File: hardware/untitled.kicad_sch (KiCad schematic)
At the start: 7 parts, among them U2 H5TQ4G63EFR

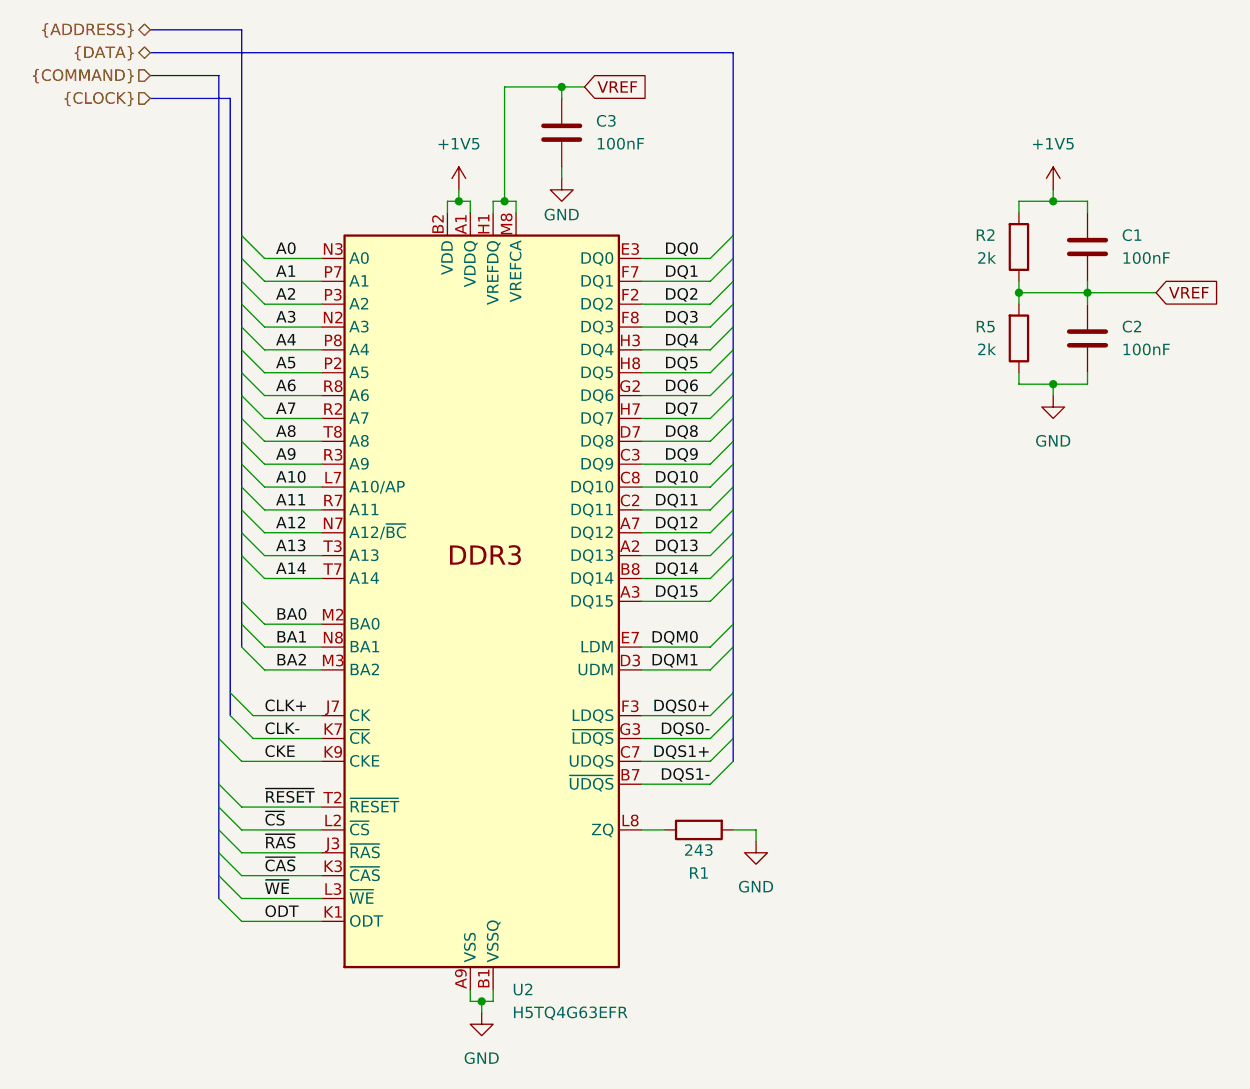
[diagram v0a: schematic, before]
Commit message: Added A13 line to DDR3
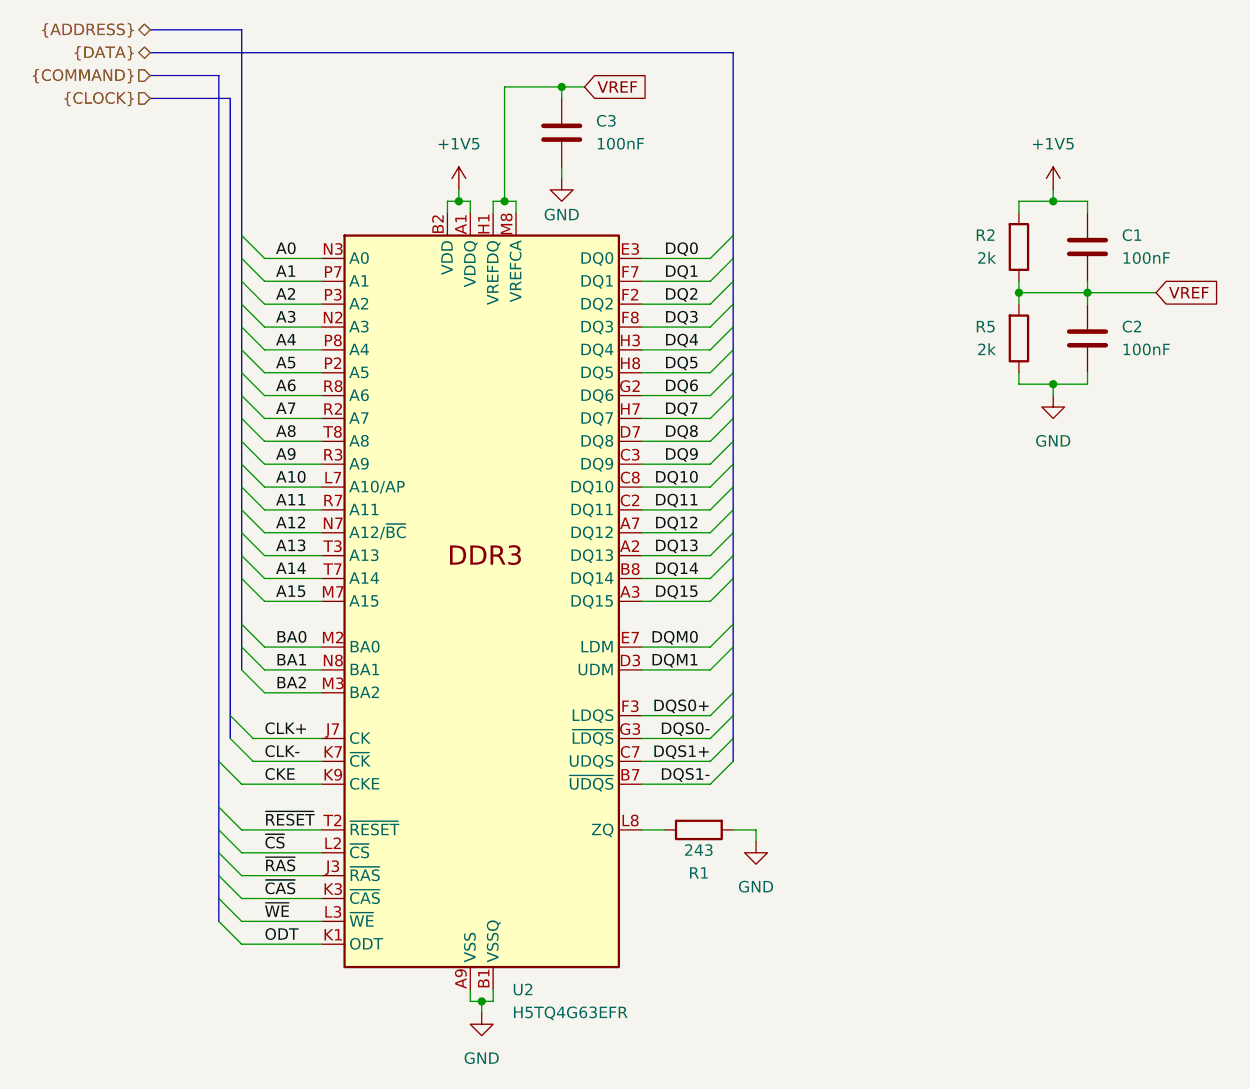
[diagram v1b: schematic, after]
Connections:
- net A15: now reaches U2.M7 (A15)
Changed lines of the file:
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@@
 	(paper "A4")
 	(bus_alias "ADDRESS"
-		(members "A[0..14]" "BA[0..2]")
+		(members "A[0..15]" "BA[0..2]")
 	)
 	(bus_alias "CLOCK"
@@
 	)
 	(bus_entry
-		(at 55.88 107.95)
+		(at 55.88 110.49)
 		(size -2.54 -2.54)
 		(stroke
@@
 	)
 	(bus_entry
-		(at 55.88 105.41)
+		(at 55.88 107.95)
 		(size -2.54 -2.54)
 		(stroke
@@
 	)
 	(bus_entry
-		(at 54.61 115.57)
+		(at 54.61 118.11)
 		(size -2.54 -2.54)
 		(stroke
@@
 	)
 	(bus_entry
-		(at 54.61 123.19)
+		(at 54.61 125.73)
 		(size -2.54 -2.54)
 		(stroke
@@
 	)
 	(bus_entry
-		(at 54.61 125.73)
+		(at 54.61 128.27)
 		(size -2.54 -2.54)
 		(stroke
@@
 	)
 	(bus_entry
-		(at 54.61 110.49)
+		(at 54.61 113.03)
 		(size -2.54 -2.54)
 		(stroke
@@
 	)
 	(bus_entry
-		(at 57.15 97.79)
+		(at 57.15 100.33)
 		(size -2.54 -2.54)
 		(stroke
@@
 	)
 	(bus_entry
-		(at 57.15 100.33)
+		(at 57.15 102.87)
 		(size -2.54 -2.54)
 		(stroke
@@
 	)
 	(bus_entry
-		(at 54.61 118.11)
+		(at 54.61 120.65)
 		(size -2.54 -2.54)
 		(stroke
@@
 	)
 	(bus_entry
-		(at 54.61 128.27)
+		(at 54.61 130.81)
+		(size -2.54 -2.54)
+		(stroke
+			(width 0)
+			(type default)
+		)
+	)
+	(bus_entry
+		(at 57.15 92.71)
 		(size -2.54 -2.54)
 		(stroke
@@
 	)
 	(bus_entry
-		(at 54.61 120.65)
+		(at 54.61 123.19)
 		(size -2.54 -2.54)
 		(stroke
@@
 	)
 	(bus_entry
-		(at 57.15 95.25)
+		(at 57.15 97.79)
 		(size -2.54 -2.54)
 		(stroke
@@
 	(wire
 		(pts
-			(xy 54.61 120.65) (xy 63.5 120.65)
+			(xy 54.61 123.19) (xy 63.5 123.19)
 		)
 		(stroke
@@
 	(bus
 		(pts
-			(xy 53.34 105.41) (xy 53.34 102.87)
+			(xy 53.34 107.95) (xy 53.34 105.41)
 		)
 		(stroke
@@
 	(wire
 		(pts
-			(xy 57.15 100.33) (xy 63.5 100.33)
+			(xy 57.15 102.87) (xy 63.5 102.87)
 		)
 		(stroke
@@
 	(wire
 		(pts
-			(xy 54.61 115.57) (xy 63.5 115.57)
+			(xy 54.61 118.11) (xy 63.5 118.11)
+		)
+		(stroke
+			(width 0)
+			(type default)
+		)
+	)
+	(wire
+		(pts
+			(xy 57.15 92.71) (xy 63.5 92.71)
 		)
 		(stroke
@@
 	(wire
 		(pts
-			(xy 57.15 95.25) (xy 63.5 95.25)
+			(xy 57.15 97.79) (xy 63.5 97.79)
 		)
 		(stroke
@@
 	(wire
 		(pts
-			(xy 54.61 118.11) (xy 63.5 118.11)
+			(xy 54.61 120.65) (xy 63.5 120.65)
 		)
 		(stroke
@@
 	(wire
 		(pts
-			(xy 54.61 128.27) (xy 63.5 128.27)
-		)
-		(stroke
-			(width 0)
-			(type default)
-		)
-	)
-	(bus
-		(pts
-			(xy 52.07 107.95) (xy 52.07 34.29)
+			(xy 54.61 130.81) (xy 63.5 130.81)
 		)
 		(stroke
@@
 	(bus
 		(pts
-			(xy 52.07 123.19) (xy 52.07 120.65)
+			(xy 52.07 125.73) (xy 52.07 123.19)
 		)
 		(stroke
@@
 	(bus
 		(pts
-			(xy 52.07 115.57) (xy 52.07 113.03)
+			(xy 52.07 118.11) (xy 52.07 115.57)
 		)
 		(stroke
@@
 	(wire
 		(pts
-			(xy 54.61 110.49) (xy 63.5 110.49)
+			(xy 54.61 113.03) (xy 63.5 113.03)
 		)
 		(stroke
@@
 		)
 	)
+	(bus
+		(pts
+			(xy 54.61 97.79) (xy 54.61 100.33)
+		)
+		(stroke
+			(width 0)
+			(type default)
+		)
+	)
 	(wire
 		(pts
@@
 	(bus
 		(pts
-			(xy 52.07 120.65) (xy 52.07 118.11)
+			(xy 52.07 123.19) (xy 52.07 120.65)
 		)
 		(stroke
@@
 	(wire
 		(pts
-			(xy 54.61 123.19) (xy 63.5 123.19)
-		)
-		(stroke
-			(width 0)
-			(type default)
-		)
-	)
-	(bus
-		(pts
-			(xy 54.61 95.25) (xy 54.61 92.71)
+			(xy 54.61 125.73) (xy 63.5 125.73)
 		)
 		(stroke
@@
 	(bus
 		(pts
-			(xy 52.07 113.03) (xy 52.07 107.95)
+			(xy 54.61 97.79) (xy 54.61 95.25)
 		)
 		(stroke
@@
 		)
 	)
-	(bus
-		(pts
-			(xy 53.34 102.87) (xy 53.34 36.83)
-		)
-		(stroke
-			(width 0)
-			(type default)
-		)
-	)
 	(wire
 		(pts
@@
 		)
 	)
-	(bus
+	(wire
 		(pts
-			(xy 54.61 97.79) (xy 54.61 95.25)
+			(xy 55.88 107.95) (xy 63.5 107.95)
 		)
 		(stroke
@@
 	(wire
 		(pts
-			(xy 55.88 105.41) (xy 63.5 105.41)
+			(xy 80.01 137.16) (xy 80.01 135.89)
 		)
 		(stroke
@@
 		)
 	)
-	(wire
+	(bus
 		(pts
-			(xy 80.01 137.16) (xy 80.01 135.89)
+			(xy 53.34 36.83) (xy 53.34 105.41)
 		)
 		(stroke
@@
 	(wire
 		(pts
-			(xy 54.61 125.73) (xy 63.5 125.73)
+			(xy 54.61 128.27) (xy 63.5 128.27)
 		)
 		(stroke
@@
 	(bus
 		(pts
-			(xy 52.07 125.73) (xy 52.07 123.19)
+			(xy 52.07 128.27) (xy 52.07 125.73)
 		)
 		(stroke
@@
 	(wire
 		(pts
-			(xy 57.15 97.79) (xy 63.5 97.79)
+			(xy 57.15 100.33) (xy 63.5 100.33)
 		)
 		(stroke
@@
 	(wire
 		(pts
-			(xy 55.88 107.95) (xy 63.5 107.95)
+			(xy 55.88 110.49) (xy 63.5 110.49)
 		)
 		(stroke
@@
 	(bus
 		(pts
+			(xy 54.61 87.63) (xy 54.61 90.17)
+		)
+		(stroke
+			(width 0)
+			(type default)
+		)
+	)
+	(bus
+		(pts
 			(xy 54.61 85.09) (xy 54.61 82.55)
 		)
@@
 	(bus
 		(pts
-			(xy 52.07 118.11) (xy 52.07 115.57)
+			(xy 52.07 110.49) (xy 52.07 115.57)
+		)
+		(stroke
+			(width 0)
+			(type default)
+		)
+	)
+	(bus
+		(pts
+			(xy 52.07 120.65) (xy 52.07 118.11)
 		)
 		(stroke
@@
 		)
 	)
+	(bus
+		(pts
+			(xy 52.07 34.29) (xy 52.07 110.49)
+		)
+		(stroke
+			(width 0)
+			(type default)
+		)
+	)
 	(wire
 		(pts
@@
 	(bus
 		(pts
-			(xy 54.61 92.71) (xy 54.61 87.63)
+			(xy 54.61 95.25) (xy 54.61 90.17)
 		)
 		(stroke
@@
 	)
 	(label "BA0"
-		(at 58.42 95.25 0)
+		(at 58.42 97.79 0)
 		(effects
 			(font
@@
 	)
 	(label "~{CS}"
-		(at 57.15 118.11 0)
+		(at 57.15 120.65 0)
 		(effects
 			(font
@@
 	)
 	(label "BA2"
-		(at 58.42 100.33 0)
+		(at 58.42 102.87 0)
 		(effects
 			(font
@@
 	)
 	(label "CLK-"
-		(at 57.15 107.95 0)
+		(at 57.15 110.49 0)
 		(effects
 			(font
@@
 		)
 	)
+	(label "A15"
+		(at 58.42 92.71 0)
+		(effects
+			(font
+				(size 1.27 1.27)
+			)
+			(justify left bottom)
+		)
+	)
 	(label "A10"
 		(at 58.42 80.01 0)
@@
 	)
 	(label "~{CAS}"
-		(at 57.15 123.19 0)
+		(at 57.15 125.73 0)
 		(effects
 			(font
@@
 	)
 	(label "CKE"
-		(at 57.15 110.49 0)
+		(at 57.15 113.03 0)
 		(effects
 			(font
@@
 	)
 	(label "CLK+"
-		(at 57.15 105.41 0)
+		(at 57.15 107.95 0)
 		(effects
 			(font
@@
 	)
 	(label "~{RAS}"
-		(at 57.15 120.65 0)
+		(at 57.15 123.19 0)
 		(effects
 			(font
@@
 	)
 	(label "~{WE}"
-		(at 57.15 125.73 0)
+		(at 57.15 128.27 0)
 		(effects
 			(font
@@
 	)
 	(label "~{RESET}"
-		(at 57.15 115.57 0)
+		(at 57.15 118.11 0)
 		(effects
 			(font
@@
 	)
 	(label "ODT"
-		(at 57.15 128.27 0)
+		(at 57.15 130.81 0)
 		(effects
 			(font
@@
 	)
 	(label "BA1"
-		(at 58.42 97.79 0)
+		(at 58.42 100.33 0)
 		(effects
 			(font
